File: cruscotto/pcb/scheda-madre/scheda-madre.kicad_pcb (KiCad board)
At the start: 2 copper layers, 178.7 x 74 mm, 148 parts, among them J1 Micro-Fit 2x12 verso auto (D-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, J10 Verso P1 S3: 5V TXD RXD GND, J11 Verso P2 S3: IO19 IO11 IO12 I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, J12 Verso P6 Speak S3, J3 USB-C (solo a banco), J4 Ventola Delta AFB0412VA-00 (D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, J5 NTC display, J6 STEVAL-MKI196V1 (DIL-24), J7 Modulo MicroSD: 3V3 CS MOSI C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, J8 Modulo VAN: 3.3V GND RX TX, J9 Modulo VAN: CANH CANL, K1 G2RL-2 DC5, K2 G2RL-2 DC5, Q1 IPD50N06S4L-12 (da confermare), Q3 ZXMP6A13F (P 60 V), Q4 MMBTA06 (80 V), Q5 MMBT3904, Q6 MMBT3904, Q7 MMBT3904, Q8 MMBT5551, Q9 AO3400A, SW3 RESET, SW4 BOOT, U1 LM74700-Q1, U10 DS3231SN, U2 TPS54360B, U3 LMR36510, U4 ESP32-WROOM-32E-H4, U5 AP2112K-3.3, U6 CH340C, U7 LM2903B, U9 AP2112K-3.3

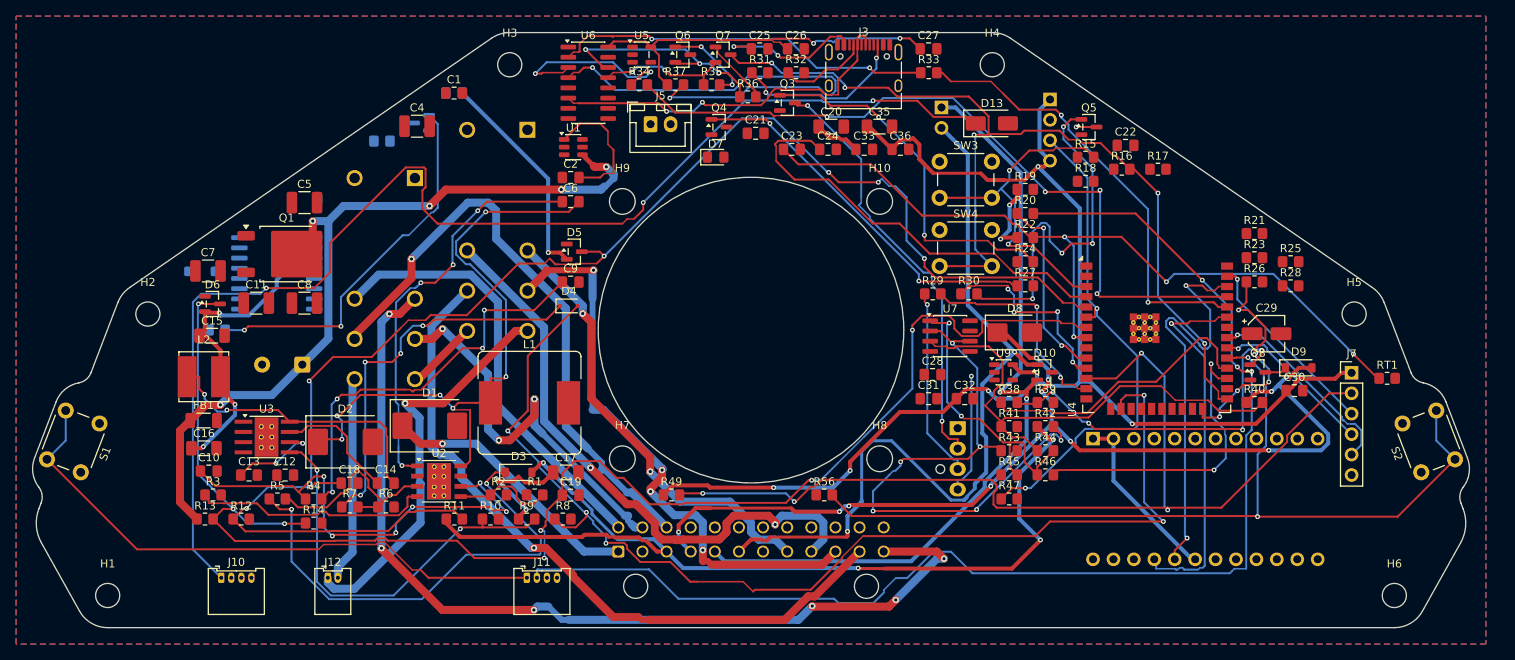
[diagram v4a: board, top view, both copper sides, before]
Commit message: feat(pcb): D-057 four-layer mainboard fully routed, DRC clean (0 errors, 0 unconnected)
- D-057: 4 copper layers (F/B parts and tracks, In1 continuous ground plane, In2 tracks + ground fill).
- D-058 fan hole lowered to the S3 centre: tried and superseded (routing got worse, 46 open
  connections); fan stays at (0; 46), J1 at the bottom edge centre.
- tools/sbroglia-scheda-madre.py: In1 exported to Specctra as a power layer (no tracks), narrower
  signal classes, In2 ground fill after routing, optional --pcb and --router.* passthrough.
- tools/completa-sbroglio-scheda-madre.py (new): fixed USB-C fan-out (alternating D+/D- pins to
  staggered vias), A* routing on a 0.05 mm grid on F/In2/B for the connections Freerouting leaves
  open, rip-up of blocking nets, ground island stitching, final KiCad DRC loop (errors and
  warnings) that removes and reroutes offending tracks and vias.
- scheda-madre.kicad_dru: one thermal spoke is enough on through-hole pads (ground via In1).
- Board: 2854 tracks (4.1 m), 468 vias; DRC 0 errors, 0 unconnected; 87 silkscreen warnings left.
- Previews sbroglio-rame-F/In2/B.png, README and docs updated.

Limits: generated routing checked only by DRC; no signal-integrity review (USB without controlled
impedance), silkscreen to tidy, no Gerbers, nothing built or tested. Freerouting runs are not
bit-for-bit reproducible (internal time limits).

Co-Authored-By: Claude Opus 5.5 <noreply@anthropic.com>
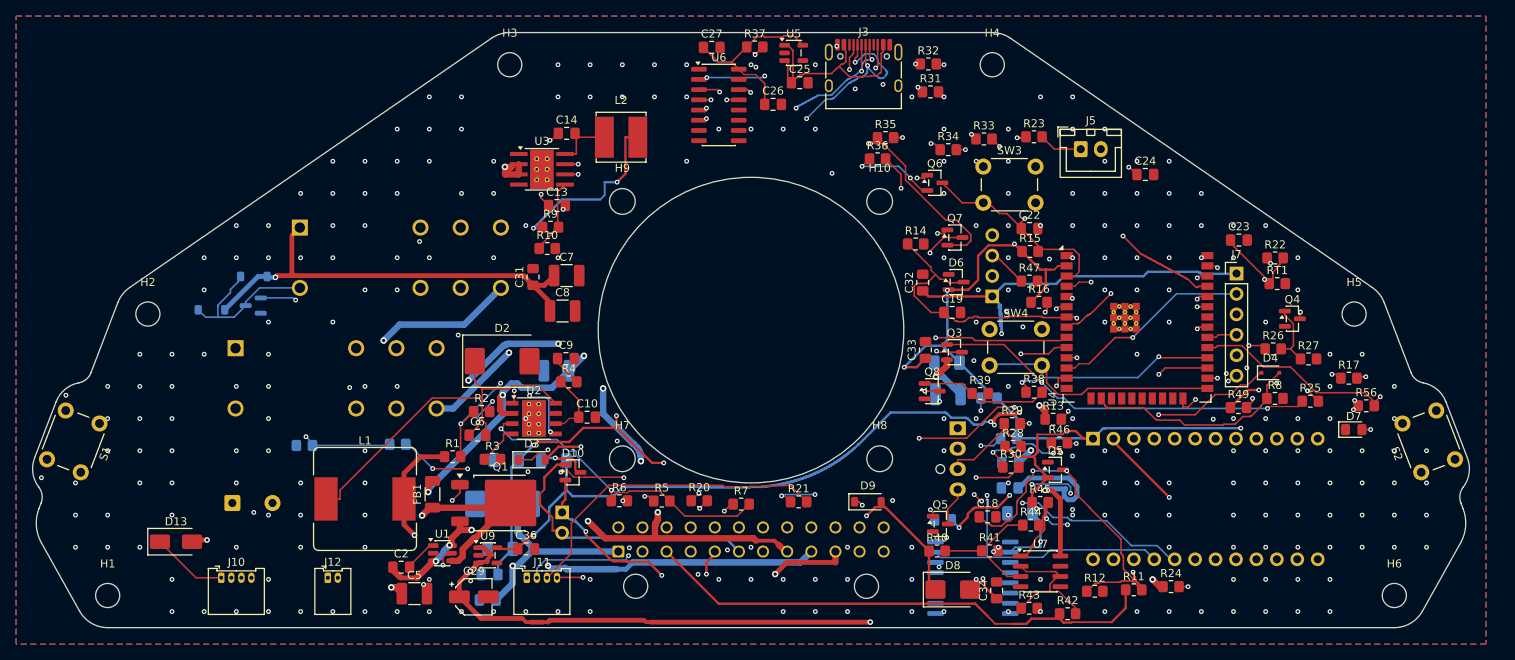
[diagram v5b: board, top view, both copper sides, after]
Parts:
- C1, C11, C12, C15, C16, C17, C20, C21, C28, C30, C35, C4, D1, R18, R19: moved to B.Cu
- C34: moved to F.Cu
- moved D13 114.0 mm to (77.0, 131.3)
- moved R12 106.5 mm to (191.3, 137.5)
- moved R13 106.2 mm to (186.1, 116.1)
- moved C29 103.9 mm to (114.0, 138.2)
- moved C15 102.9 mm to (181.9, 127.8), turned to 180 degrees
- moved U10 94.5 mm to (176.1, 135.8)
- moved C16 93.0 mm to (172.9, 109.0), turned to 180 degrees
- moved D6 92.5 mm to (174.0, 99.0)
- moved C34 91.5 mm to (179.0, 137.4), turned to 90 degrees
- moved C12 90.2 mm to (180.7, 121.5), turned to 180 degrees
- moved R8 89.8 mm to (213.7, 113.5)
- moved D4 87.6 mm to (213.1, 110.3)
- moved D7 86.3 mm to (223.4, 117.4)
- moved R11 84.9 mm to (196.1, 137.3)
- moved R14 82.5 mm to (169.0, 94.3)
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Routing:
- net +5V: track 0.00 -> 266.1 mm, vias 0 -> 6
- net +3V3_AON: track 119.5 -> 325.6 mm, vias 8 -> 17
- net +12V_F: track 0.00 -> 201.7 mm, vias 0 -> 8
- net Net-(D13-K): track 156.7 -> 9.49 mm, vias 3 -> 0
- net VBAT_SENSE: track 184.5 -> 48.1 mm, vias 7 -> 2
- net LINK_FE2S3: track 159.0 -> 29.9 mm, vias 3 -> 2
- net PWR_HOLD: track 140.5 -> 25.8 mm, vias 5 -> 0
- net KEY_SENSE: track 186.9 -> 80.3 mm, vias 7 -> 4
- net VBAT_P: track 99.6 -> 206.1 mm, vias 5 -> 2
- net KLINE: track 127.7 -> 40.4 mm, vias 11 -> 1
- net SD_CS: track 124.3 -> 40.3 mm, vias 4 -> 2
- net FE_BTN2: track 112.5 -> 40.0 mm, vias 2 -> 1
- net VAN_DATA: track 98.9 -> 27.5 mm, vias 2 -> 3
- net NTC_PCB: track 101.6 -> 35.8 mm, vias 4 -> 2
- net VAN_DATAB: track 98.5 -> 35.0 mm, vias 2 -> 0
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- added copper zone on In1.Cu, net GND
- added copper zone on In2.Cu, net GND
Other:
- copper layers 2 -> 4

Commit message: feat(pcb): D-059 wires soldered to the mainboard, re-routed; BOM with Farnell availability
- D-059: fan (J4), display NTC (J5) and S3 cables (J10-J12) on 26 AWG solder-wire pads instead of
  connectors; MicroSD, VAN and IMU modules soldered directly. Schematic sheets EL-002 rev B,
  EL-004 rev C, EL-005 rev B (27/10/2026); J11 moved 2.5 mm outward for J1 clearance.
- Placement and routing redone: 3987 tracks, 514 vias; DRC 0 errors, 0 unconnected, no hole or
  dangling warnings; 92 silkscreen warnings left.
- completa-sbroglio-scheda-madre.py: drill map so new vias keep the 0.25 mm hole-to-hole distance
  from every drill, including same-net ones.
- BOM: everything needed except consumables; parts shared with the Data Logger order flagged
  (LM2903B spare, EEEHB1C100R; second VAN and SD modules needed).
- tools/controlla-distinta-farnell.py (element14 Product Search API, key read from env or
  ~/.farnell_api_key, never printed) and the 27/10/2026 Farnell snapshot: 10 items not stocked
  (ESP32-WROOM-32E-H4, TPS54360B, LMR36510, LM74700-Q1, CH340C, AO3400A, SRR1260-8R2Y, HRO USB-C,
  7.3 mm tactile switches, AFB0412VA-00), 4 at zero stock.

Limits: routing checked only by DRC; nothing ordered, built or tested.

Co-Authored-By: Claude Opus 5.5 <noreply@anthropic.com>
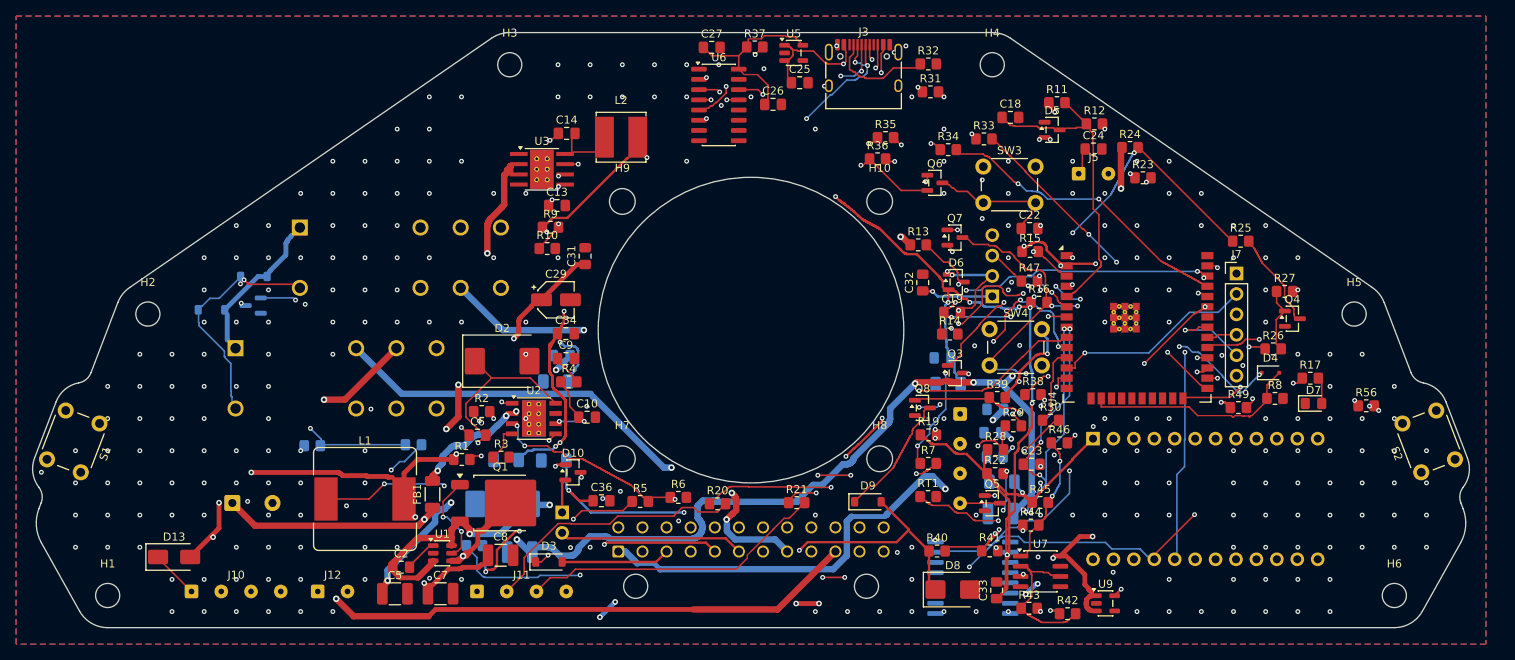
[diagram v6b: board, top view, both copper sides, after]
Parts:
- J10, J11: footprint Molex_PicoBlade_53048-0410_1x04_P1.25mm_Horizontal -> SolderWire-0.127sqmm_1x04_P3.7mm_D0.48mm_OD1mm
- J12: footprint Molex_PicoBlade_53048-0210_1x02_P1.25mm_Horizontal -> SolderWire-0.127sqmm_1x02_P3.7mm_D0.48mm_OD1mm
- J4: footprint FanPinHeader_1x04_P2.54mm_Vertical -> SolderWire-0.127sqmm_1x04_P3.7mm_D0.48mm_OD1mm
- J5: footprint JST_XH_B2B-XH-A_1x02_P2.50mm_Vertical -> SolderWire-0.127sqmm_1x02_P3.7mm_D0.48mm_OD1mm
- R19: moved to F.Cu
- moved U9 77.1 mm to (192.6, 139.0)
- moved C1 67.4 mm to (178.9, 114.9)
- moved R18 66.6 mm to (114.1, 131.8)
- moved C15 64.2 mm to (118.1, 121.1)
- moved C21 62.4 mm to (172.3, 108.5)
- moved C34 62.4 mm to (125.5, 105.4), turned to 0 degrees
- moved R11 61.3 mm to (186.5, 76.7)
- moved C20 59.3 mm to (173.0, 111.7)
- moved R12 58.1 mm to (191.2, 79.4)
- moved C11 58.0 mm to (179.5, 127.8)
- moved C12 57.3 mm to (125.0, 108.2)
- moved C4 56.7 mm to (119.7, 132.6)
- moved R24 54.8 mm to (195.6, 82.3)
- moved RT1 50.9 mm to (170.5, 125.7)
- moved C18 49.8 mm to (180.8, 78.5)
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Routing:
- net I2C_SDA: track 83.1 -> 172.4 mm, vias 3 -> 8
- net VBAT_IN: track 47.5 -> 108.4 mm
- net KEY_SENSE: track 80.3 -> 33.0 mm, vias 4 -> 0
- net KEY_IN: track 88.5 -> 134.3 mm, vias 1 -> 2
- net NTC_PCB: track 35.8 -> 73.3 mm, vias 2 -> 9
- net VBAT_P: track 206.1 -> 171.0 mm, vias 2 -> 3
- net SPK_L_P: track 75.4 -> 103.6 mm, vias 1 -> 2
- net Net-(Q3-G): track 77.3 -> 50.7 mm
- net RADIO_R_P: track 89.4 -> 113.1 mm
- net VBAT_SENSE: track 48.1 -> 24.5 mm, vias 2 -> 5
- net +12V_F: track 201.7 -> 221.0 mm, vias 8 -> 14
- net RADIO_L_P: track 85.9 -> 67.3 mm, vias 6 -> 3
- net RADIO_R_N: track 40.9 -> 59.1 mm
- net Net-(U2-EN): track 39.6 -> 55.5 mm, vias 2 -> 6
- net FAN_PWM: track 24.9 -> 9.63 mm, vias 3 -> 0
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
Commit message: feat(bom): S1/S2 Omron B3F-1050, Vishay NTCs with datasheet B value; LCSC cart cross-check
- S1/S2 = Omron B3F-1050 (6x6, 7.3 mm, 100 gf); RT1 = Vishay NTCS0805E3104FXT; display NTC = Vishay
  NTCLE100E3104JB0 (leaded). B value from the datasheets, to be used by the firmware (not B3950).
  Schematic EL-002/EL-005 values and board values updated; footprints unchanged, routing still valid
  (DRC 0 errors, 0 unconnected).
- BOM: LCSC cart of 28/10/2026 (86.37 USD + 13 USD shipping) covers most parts; Q1, L1, C3, R5, R38,
  fan, 22 uF 1206, 10k and 100k from other suppliers; prefer original Diodes AP2112K over the clone.

Co-Authored-By: Claude Opus 5.5 <noreply@anthropic.com>
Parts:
- RT1: value NTC 100k B3950 -> NTCS0805E3104FXT
- S1, S2: value Tattile 6x6 H7,3 (pulsante quadro) -> B3F-1050
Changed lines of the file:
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@@
 			)
 		)
-		(property "Value" "NTC 100k B3950"
+		(property "Value" "NTCS0805E3104FXT"
 			(at 0 1.65 0)
 			(layer "F.Fab")
@@
 			)
 		)
-		(property "Value" "Tattile 6x6 H7,3 (pulsante quadro)"
+		(property "Value" "B3F-1050"
 			(at 3.75 6.7 111)
 			(layer "F.Fab")
@@
 			)
 		)
-		(property "Value" "Tattile 6x6 H7,3 (pulsante quadro)"
+		(property "Value" "B3F-1050"
 			(at 3.75 6.7 249)
 			(layer "F.Fab")
